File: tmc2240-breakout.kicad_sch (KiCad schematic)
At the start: 30 parts, among them J1 Conn_01x04_Pin, J2 Conn_01x05_Pin, Q1 NMOS, Q2 NMOS, U1 TMC2240ATJ+

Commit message: did more stuff
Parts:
- removed Q1: NMOS, symbol Simulation_SPICE:NMOS
- removed R5: 10k, symbol Device:R
- added C11: 100nF 50V, symbol Device:C
- added C12: 10uF 6.3V, symbol Device:C
- added C13: 22nF 50V, symbol Device:C
- added C14: 1uF 50V, symbol Device:C
- added D2, D5: GREEN, symbol Device:LED
- added D3, D4: BLUE, symbol Device:LED
- added J3, J4: Conn_01x02, symbol Connector_Generic:Conn_01x02
- added Q10, Q11, Q12, Q13, Q14, Q3, Q5, Q6, Q7, Q8, Q9: NMOS, symbol Simulation_SPICE:NMOS
- added R10, R11, R12, R13, R14, R15, R16, R17, R18, R19, R22, R23, R24, R26, R9: 24k, symbol Device:R
- added R20, R21, R25, R27, R7: R, symbol Device:R
- added R8: 100k, symbol Device:R
- added TP10, TP11, TP12, TP13, TP14, TP15, TP16, TP17, TP9: TestPoint, symbol Connector:TestPoint
- added U2: LD1117S18TR_SOT223, Package_TO_SOT_SMD:SOT-223-3_TabPin2, symbol Regulator_Linear:LD1117S18TR_SOT223
- D1: value LED -> RED
- R4: value 10k -> 0
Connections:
- net OV_AH is gone; now on net OV: Q2.2 (G)
- net +1V8: now also C12.1, U2.2 (VO)
- net +3.3V: now also C11.1, J3.1 (Pin_1), J4.1 (Pin_1), R10.1, R12.1, R18.1, R19.1, R20.1, R24.1, R25.1, R26.1, R27.1, R7.1, R8.1, R9.1, U2.3 (VI); no longer R4.1
- net GND: now also R4.2, C11.2, C12.2, Q10.3 (S), Q11.3 (S), Q12.3 (S), Q13.3 (S), Q14.3 (S), Q3.3 (S), Q5.3 (S), Q6.3 (S), Q7.3 (S), Q8.3 (S), Q9.3 (S), R11.2, R16.2, R22.2, R23.2, U2.1 (GND)
- net VMOTOR: now reaches C1.1, C2.1, C3.1, C4.1, C5.1, C6.1, C8.1, C9.1, U1.17 (VS), U1.20 (VS), U1.21 (VS), U1.24 (VS)
- net VMOTOR: now also C14.2, R21.1
- net IREF: now reaches U1.1 (IREF)
- net IREF: now also R13.1, R14.1, R15.1, TP17.1
- net UART_EN: now reaches U1.10 (UART_EN)
- net UART_EN: now also R10.2, R11.1, TP13.1
- net DIAG0#: now reaches U1.11 (DIAG0)
- net DIAG0#: now also Q10.2 (G), TP15.1
- net DIAG1#: now reaches U1.12 (DIAG1/SW)
- net DIAG1#: now also Q13.2 (G), TP16.1
- net CPI: now reaches U1.14 (CPI)
- net CPI: now also C13.1
- net CPO: now reaches U1.15 (CPO)
- net CPO: now also C13.2
- net at U1.16 (VCP): now also C14.1
- net SLEEP#: now reaches U1.25 (SLEEPN)
- net SLEEP#: now also R12.2, TP14.1
- net at U1.30 (CLK): now also R4.1
- net STEP: now reaches U1.31 (STEP)
- net STEP: now also TP9.1
- net DIR: now reaches U1.32 (DIR)
- net DIR: now also TP10.1
- net DRV_EN#: now reaches U1.9 (DRV_ENN)
- net DRV_EN#: now also Q6.2 (G), R8.2, TP11.1
- net OV# renamed OV
- net OV: now also Q9.2 (G), R9.2, TP12.1; no longer R4.2
- new net: D4.1 (K), Q12.1 (D)
- new net: Q9.1 (D), R21.2
- new net: D2.2 (A), R7.2
- new net: D4.2 (A), R25.2
- new net: Q3.1 (D), R15.2
- new net: Q11.1 (D), R17.2
- new net: R14.2, R17.1
- new net: R13.2, R16.1
- new net: D5.1 (K), Q14.1 (D)
- new net: D5.2 (A), R27.2
- new net: D2.1 (K), Q5.1 (D)
- new net: D3.1 (K), Q8.1 (D)
- new net: D3.2 (A), R20.2
- new net DIAG0: Q10.1 (D), Q12.2 (G), R24.2
- new net DIAG1_AH: Q13.1 (D), Q14.2 (G), R26.2
- new net EN_AH: Q5.2 (G), Q6.1 (D), Q7.1 (D), Q8.2 (G), R18.2, R19.2
- new net IREF_R2: J3.2 (Pin_2), Q3.2 (G), R23.1
- new net IREF_R3: J4.2 (Pin_2), Q11.2 (G), R22.1
- new net SLEEP_EN#: Q7.2 (G)
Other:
- note added: "Debugging LEDs"
- moved on the sheet: D1, J1, J2, Q2, R1, R2, R3, R6, TP1, TP2, TP3, TP4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

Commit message: did some minor things, organized schematic a bit
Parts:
- added H1, H2, H3, H4: MountingHole, symbol Mechanical:MountingHole
- added J5: Conn_01x15, symbol Connector_Generic:Conn_01x15
- added TP18, TP19: TestPoint, symbol Connector:TestPoint
- added TP20, TP21: TestPoint_Alt, symbol Connector:TestPoint_Alt
- D4: value BLUE -> RED
- D5: value GREEN -> RED
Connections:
- net +1V8: now also TP19.1
- net +3.3V: now also TP18.1
- net DIAG0#: now also J5.11 (Pin_11)
- net DIAG1#: now also J5.12 (Pin_12)
- net DIR: now also J5.6 (Pin_6)
- net DRV_EN#: now also J5.7 (Pin_7)
- net GND: now also TP20.1, TP21.1
- net IREF: now also J5.13 (Pin_13)
- net IREF_R2: now also J5.14 (Pin_14)
- net IREF_R3: now also J5.15 (Pin_15)
- net OV: now also J5.8 (Pin_8)
- net SLEEP#: now also J5.10 (Pin_10)
- net SPI_CS#: now also J5.4 (Pin_4)
- net SPI_SCK: now also J5.1 (Pin_1)
- net SPI_SDI: now also J5.2 (Pin_2)
- net SPI_SDO: now also J5.3 (Pin_3)
- net STEP: now also J5.5 (Pin_5)
- net UART_EN: now also J5.9 (Pin_9)
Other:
- note added: "1.8 V LDO"
- note added: "CAD Note: IREF_R2 & IREF_R3 In silkscreen"
- note added: "CAD Note: Label LEDs in silkscreen"
- note added: "Design Note: DRV_EN default disabled, MCU should actively enable UART_EN default disabled, SPI default SLEEP# default disabled"
- note added: "IREF Control"
- note added: "OV Protection Resistor"
- note added: "TODO: set OV breaking resistor"
- moved on the sheet: C11, C12, J3, J4, Q11, Q3, R13, R14, R15, R16, R17, R22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

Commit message: did a lot of sourcing of lcsc, most is basic
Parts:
- C1, C11, C2, C3, C4, C7: footprint (none) -> Capacitor_SMD:C_0402_1005Metric; LCSC (none) -> C307331
- C10: value 2.2uF 6.3V -> 2.2uF 16V; footprint (none) -> Capacitor_SMD:C_0603_1608Metric; LCSC (none) -> C23630
- C12: value 10uF 6.3V -> 10uF 10V; footprint (none) -> Capacitor_SMD:C_0603_1608Metric; LCSC (none) -> C19702
- C13: footprint (none) -> Capacitor_SMD:C_0402_1005Metric; LCSC (none) -> C1532
- C14, C5, C6: footprint (none) -> Capacitor_SMD:C_0603_1608Metric; LCSC (none) -> C15849
- D1, D4, D5: footprint (none) -> LED_SMD:LED_0805_2012Metric; LCSC (none) -> C84256
- D2: footprint (none) -> LED_SMD:LED_0805_2012Metric; LCSC (none) -> C2297
- D3: value BLUE -> WHITE; footprint (none) -> LED_SMD:LED_0805_2012Metric; LCSC (none) -> C34499
- H1, H2, H3, H4: footprint (none) -> MountingHole:MountingHole_3.2mm_M3; now not fitted
- J1: LCSC (none) -> C5160921
- J2: LCSC (none) -> C2908614
- J3, J4: LCSC (none) -> C7429641; now left out of the parts list
- J5: now left out of the parts list
- Q10, Q11, Q12, Q13, Q14, Q2, Q3, Q5, Q6, Q7, Q8, Q9: value NMOS -> 2N7002; LCSC (none) -> C8545
- R1, R2, R3, R8: LCSC (none) -> C25530
- R10, R11, R12, R13, R14, R15, R16, R17, R18, R19, R22, R23, R24, R26, R9: LCSC (none) -> C23352
- R4: LCSC (none) -> C60485
- TP1, TP10, TP11, TP12, TP13, TP14, TP15, TP16, TP17, TP18, TP19, TP2, TP20, TP21, TP3, TP4, TP5, TP6, TP7, TP8, TP9: now not fitted; now left out of the parts list
- U1: LCSC (none) -> C7429724
- U2: LCSC (none) -> C80598
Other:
- note added: "Decoupling caps"
- note added: "TODO: GND in motor conn?"
- note added: "TODO: add separate footprint for straight up JST-XH and support both"
- note added: "TODO: this mosfet should probably be higher current"

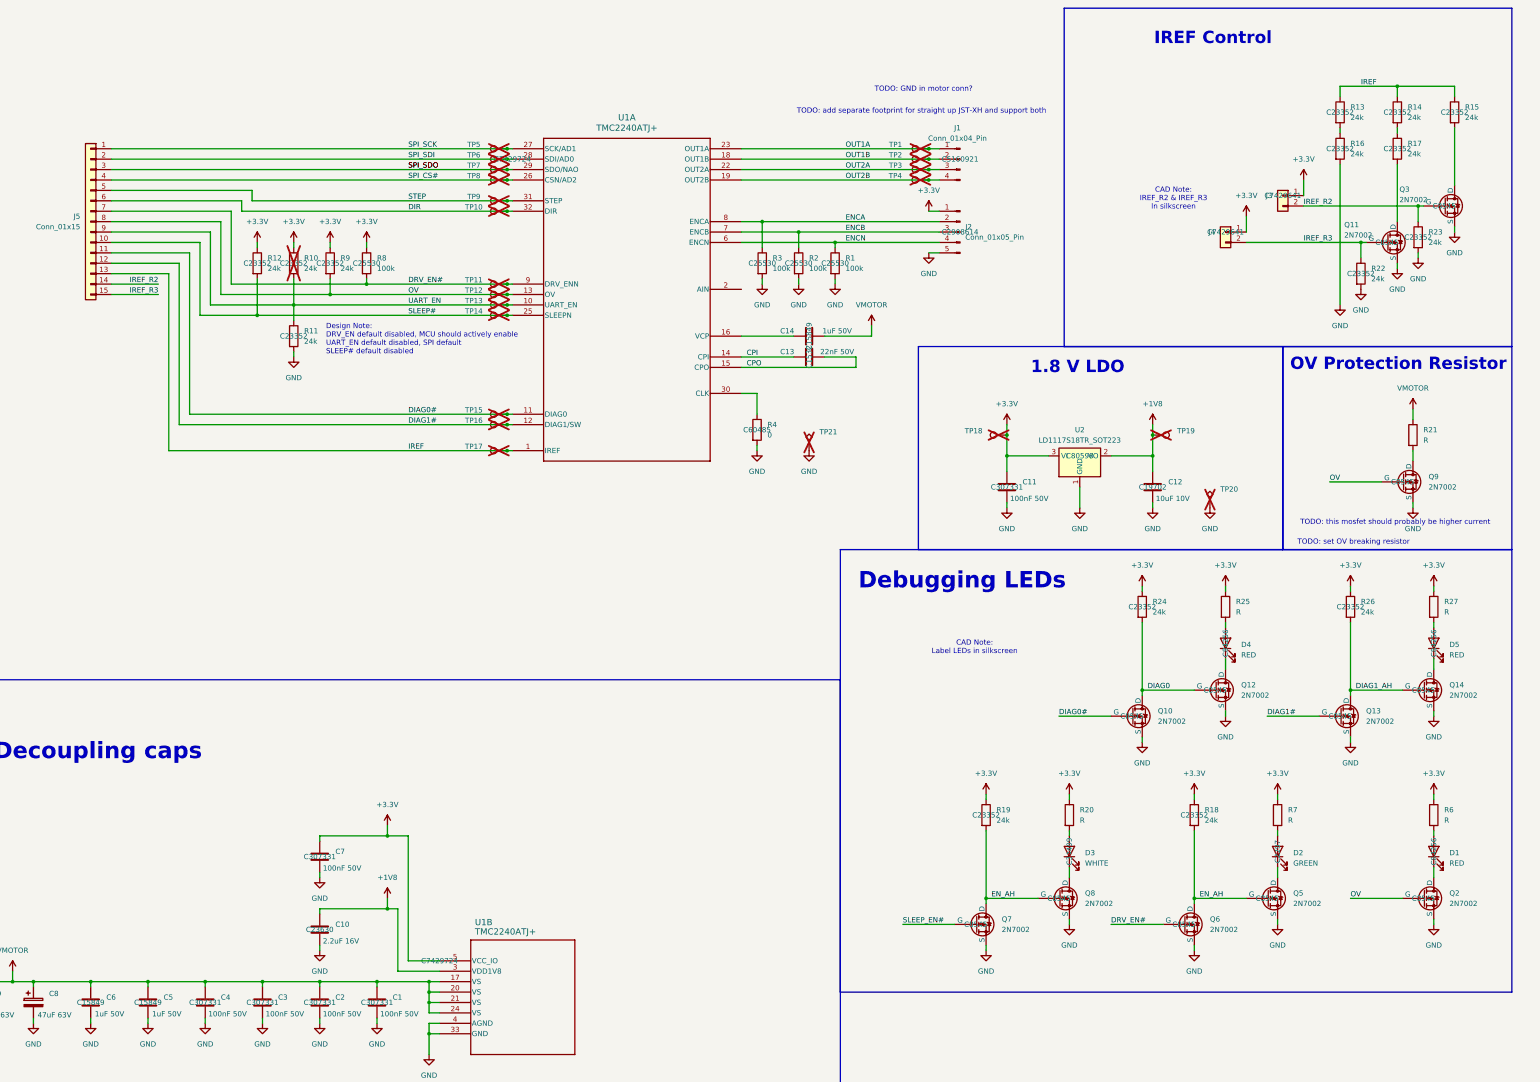
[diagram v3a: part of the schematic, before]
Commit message: did more sourcing and footprints
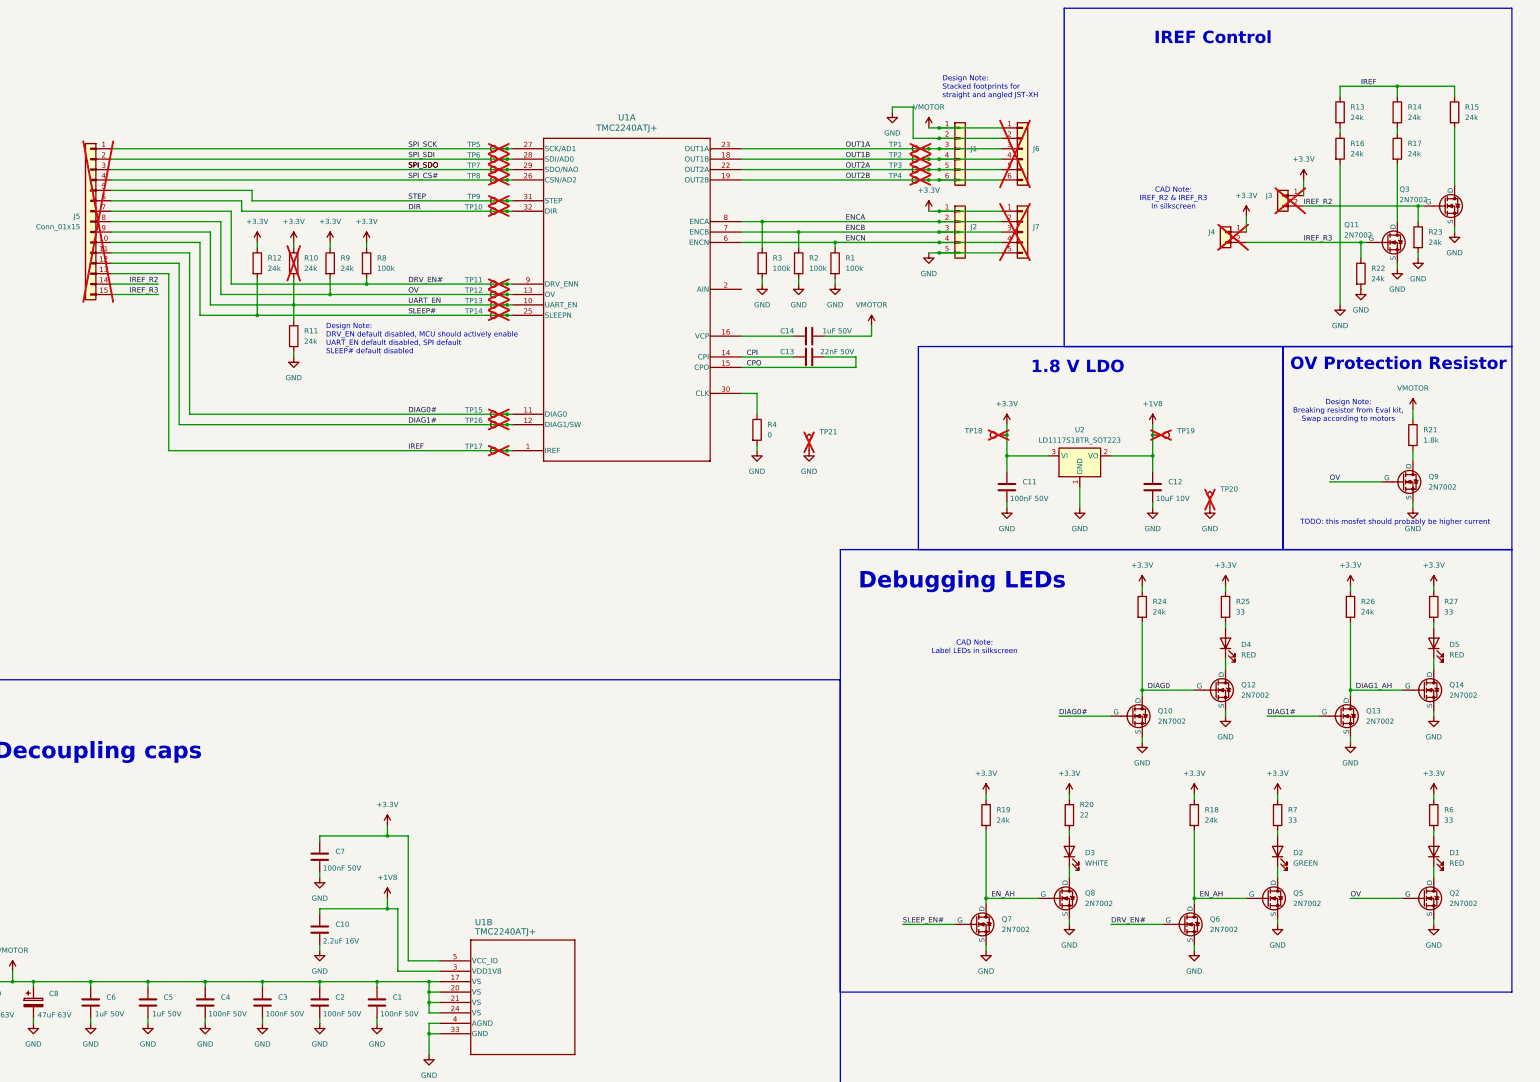
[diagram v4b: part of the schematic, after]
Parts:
- removed J1: Conn_01x04_Pin, symbol Connector:Conn_01x04_Pin
- removed J2: Conn_01x05_Pin, symbol Connector:Conn_01x05_Pin
- added J1, J6: Conn_01x06, symbol Connector_Generic:Conn_01x06
- added J2, J7: Conn_01x05, symbol Connector_Generic:Conn_01x05
- C8, C9: footprint (none) -> Capacitor_SMD:CP_Elec_6.3x7.7; LCSC (none) -> C72523
- J3, J4, J5: now not fitted
- R1, R2, R3, R4, R8: footprint (none) -> Resistor_SMD:R_0402_1005Metric
- R10, R11, R12, R13, R14, R15, R16, R17, R18, R19, R22, R23, R24, R26, R9: footprint (none) -> Resistor_SMD:R_0201_0603Metric
- R20: value R -> 22; footprint (none) -> Resistor_SMD:R_0402_1005Metric; LCSC (none) -> C25092
- R21: value R -> 1.8k; footprint (none) -> Resistor_SMD:R_2512_6332Metric; LCSC (none) -> C137011
- R25, R27, R6, R7: value R -> 33; footprint (none) -> Resistor_SMD:R_0402_1005Metric; LCSC (none) -> C25105
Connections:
- net +3.3V: now also J2.1 (Pin_1), J7.1 (Pin_1)
- net ENCA: now also J2.2 (Pin_2), J7.2 (Pin_2)
- net ENCB: now also J2.3 (Pin_3), J7.3 (Pin_3)
- net ENCN: now also J2.4 (Pin_4), J7.4 (Pin_4)
- net GND: now also J1.2 (Pin_2), J2.5 (Pin_5), J6.2 (Pin_2), J7.5 (Pin_5)
- net OUT1A: now also J1.3 (Pin_3), J6.3 (Pin_3)
- net OUT1B: now also J1.4 (Pin_4), J6.4 (Pin_4)
- net OUT2A: now also J1.5 (Pin_5), J6.5 (Pin_5)
- net OUT2B: now also J1.6 (Pin_6), J6.6 (Pin_6)
- net VMOTOR: now also J1.1 (Pin_1), J6.1 (Pin_1)
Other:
- note added: "Design Note: Breaking resistor from Eval kit, Swap according to motors"
- note added: "Design Note: Stacked footprints for straight and angled JST-XH"
- note removed: "TODO: GND in motor conn?"
- note removed: "TODO: add separate footprint for straight up JST-XH and support both"
- note removed: "TODO: set OV breaking resistor"
